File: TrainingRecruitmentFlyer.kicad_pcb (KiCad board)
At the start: 2 copper layers, 59.7 x 95.5 mm, 188 parts, among them SW1 3P1T_Fused, U1 VNH5019A-E, U10 LS_4, U2 VNH5019A-E, U3 3.3V_OKI, U4 LS_1, U5 LS_2, U6 TM4C129E_Launchpad_X9, U7 Picoblade-3, U8 Picoblade-3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

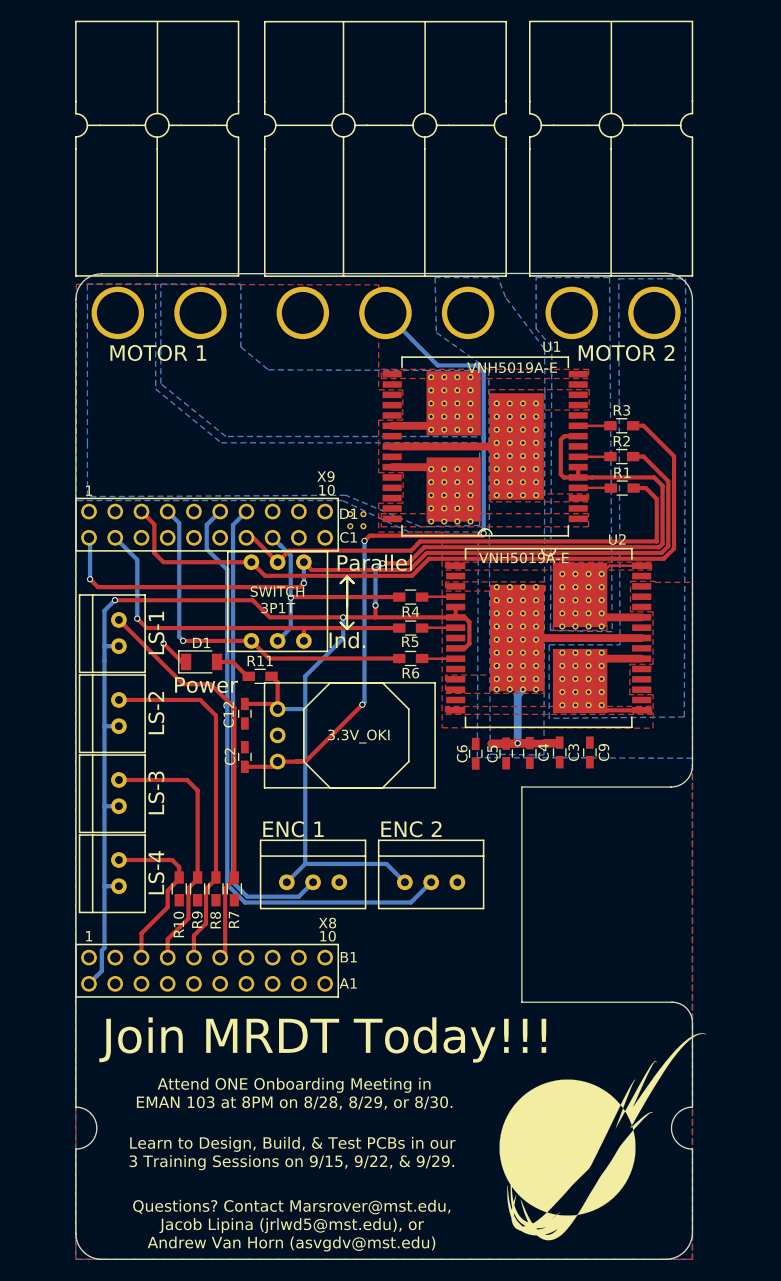
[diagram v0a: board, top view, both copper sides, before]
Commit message: Updated silkscreen, renamed files
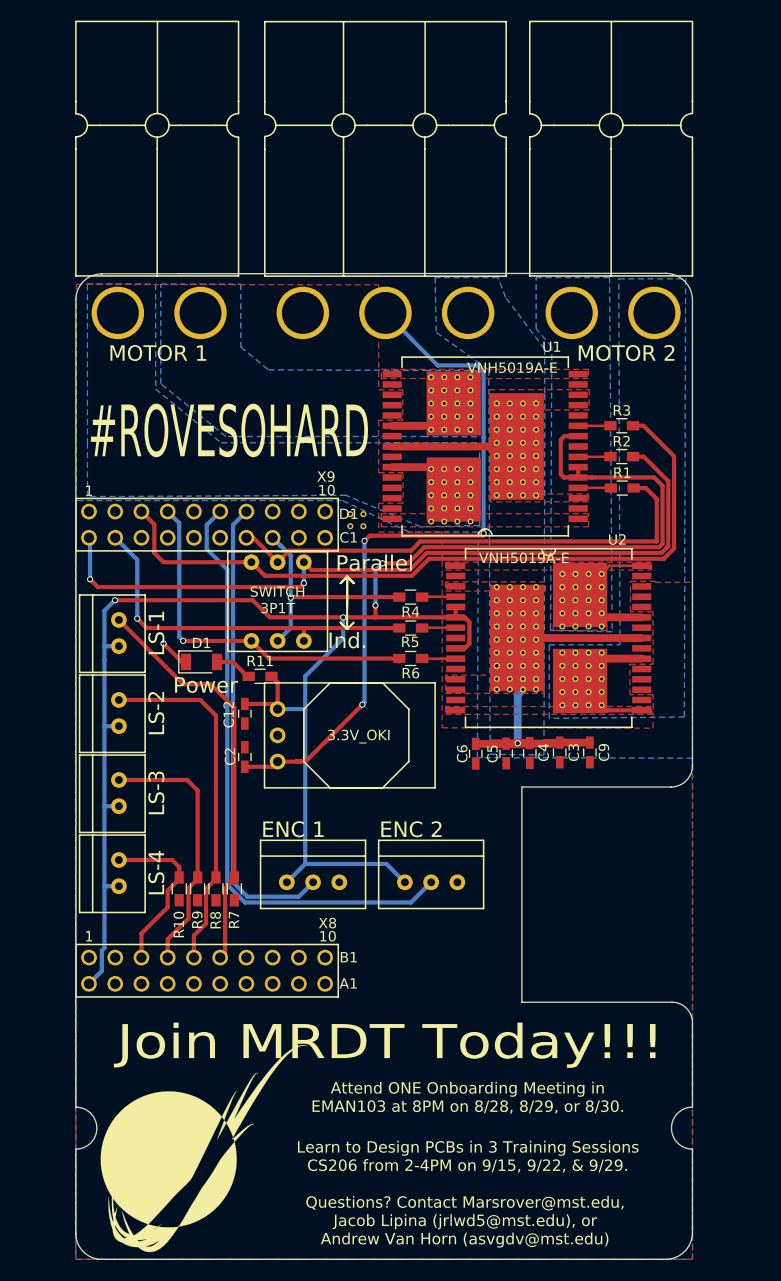
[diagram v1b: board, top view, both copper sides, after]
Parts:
- moved G*** 38.6 mm to (130.4, 223.3)
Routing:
- net +12V: track 41.0 -> 45.4 mm
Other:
- board text added: "#ROVESOHARD"
- board text added: "Attend ONE Onboarding Meeting in EMAN103 at 8PM on 8/28, 8/29, or 8/30."
- board text added: "Learn to Design PCBs in 3 Training Sessions CS206 from 2-4PM on 9/15, 9/22, & 9/29."
- board text added: "MARS ROVER DESIGN TEAM"
- board text added: "Today. Tomorrow. Forever."
- board text removed: "Attend ONE Onboarding Meeting in EMAN 103 at 8PM on 8/28, 8/29, or 8/30."
- board text removed: "Learn to Design, Build, & Test PCBs in our 3 Training Sessions on 9/15, 9/22, & 9/29."
- board text removed: "MARS ROVER DESIGN TEAM Today. Tomorrow. Forever"
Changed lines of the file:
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@@
 (kicad_pcb (version 4) (host pcbnew 4.0.7)
   (general
-    (links 0)
+    (links 259)
     (no_connects 2)
-    (area 117.958399 138.481599 177.748401 234.034801)
+    (area 116.32154 81.433999 192.4064 235.47846)
     (thickness 1.6)
-    (drawings 61)
-    (tracks 261)
+    (drawings 63)
+    (tracks 264)
     (zones 0)
     (modules 188)
@@
   )
   (setup
-    (last_trace_width 0.25)
+    (last_trace_width 0.762)
     (user_trace_width 0.254)
     (user_trace_width 0.4064)
@@
   )
   (module MRDT_Silkscreens:MRDT_Logo_20mm (layer F.Cu)
-    (at 169.037 222.123)
+    (at 130.429 223.266)
     (tags "Logo, MRDT")
     (fp_text reference G*** (at -3.6068 11.8364) (layer Dwgs.User) hide
@@
       (xy 9.693896 -10.010636)) (layer F.SilkS) (width 0.01))
   )
-  (gr_text "Questions? Contact Marsrover@mst.edu,\nJacob Lipina (jrlwd5@mst.edu), or\nAndrew Van Horn (asvgdv@mst.edu)" (at 138.938 230.632) (layer F.SilkS)
+  (gr_text "Today. Tomorrow. Forever." (at 147.955 157.226) (layer B.SilkS)
+    (effects (font (size 3 2.9) (thickness 0.3)) (justify mirror))
+  )
+  (gr_text "#ROVESOHARD" (at 132.842 153.924) (layer F.SilkS)
+    (effects (font (size 5 2.5) (thickness 0.3)))
+  )
+  (gr_text "Questions? Contact Marsrover@mst.edu,\nJacob Lipina (jrlwd5@mst.edu), or\nAndrew Van Horn (asvgdv@mst.edu)" (at 155.702 230.251) (layer F.SilkS)
     (effects (font (size 1.1 1.1) (thickness 0.275)))
   )
-  (gr_text "Learn to Design, Build, & Test PCBs in our\n3 Training Sessions on 9/15, 9/22, & 9/29." (at 138.938 223.647) (layer F.SilkS)
+  (gr_text "Learn to Design PCBs in 3 Training Sessions\nCS206 from 2-4PM on 9/15, 9/22, & 9/29." (at 155.956 224.028) (layer F.SilkS)
     (effects (font (size 1.1 1.1) (thickness 0.275)))
   )
-  (gr_text "Attend ONE Onboarding Meeting in\nEMAN 103 at 8PM on 8/28, 8/29, or 8/30." (at 139.192 217.932) (layer F.SilkS)
+  (gr_text "Attend ONE Onboarding Meeting in\nEMAN103 at 8PM on 8/28, 8/29, or 8/30." (at 155.956 218.313) (layer F.SilkS)
     (effects (font (size 1.1 1.1) (thickness 0.25)))
   )
-  (gr_text "Join MRDT Today!!!" (at 142.367 212.471) (layer F.SilkS)
-    (effects (font (size 3.3 3.3) (thickness 0.3)))
+  (gr_text "Join MRDT Today!!!" (at 148.463 212.979) (layer F.SilkS)
+    (effects (font (size 3.3 4) (thickness 0.3)))
   )
-  (gr_text "MARS ROVER DESIGN TEAM\nToday. Tomorrow. Forever" (at 147.574 153.924) (layer B.SilkS)
-    (effects (font (size 2.9 2.9) (thickness 0.3)) (justify mirror))
+  (gr_text "MARS ROVER DESIGN TEAM" (at 147.828 151.765) (layer B.SilkS)
+    (effects (font (size 5 2.9) (thickness 0.3)) (justify mirror))
   )
   (gr_text ACT (at 156.083 146.304) (layer B.SilkS)
@@
   (segment (start 155.65501 171.837599) (end 154.7749 171.837599) (width 0.4064) (layer F.Cu) (net 2))
   (segment (start 154.7749 170.837601) (end 154.7749 171.837599) (width 0.4064) (layer F.Cu) (net 2))
+  (segment (start 164.846 183.962) (end 167.767 183.962) (width 0.762) (layer F.Cu) (net 3))
+  (segment (start 158.242 184.0636) (end 158.2166 184.089) (width 0.762) (layer F.Cu) (net 3))
+  (segment (start 158.2166 184.089) (end 156.718 184.089) (width 0.762) (layer F.Cu) (net 3))
   (segment (start 158.242 184.0636) (end 159.6644 184.0636) (width 0.762) (layer F.Cu) (net 3))
   (segment (start 159.6644 184.0636) (end 160.7414 184.0636) (width 0.762) (layer F.Cu) (net 3))

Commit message: Changed text to pass ACT
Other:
- board text added: "Learn to Design PCBs in THREE Sessions CS206 from 2-4PM on 9/15, 9/22, & 9/29."
- board text removed: "Learn to Design PCBs in 3 Training Sessions CS206 from 2-4PM on 9/15, 9/22, & 9/29."
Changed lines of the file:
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@@
   (general
     (links 259)
-    (no_connects 2)
-    (area 116.32154 81.433999 192.4064 235.47846)
+    (no_connects 0)
+    (area 116.32154 81.433999 192.4064 236.62146)
     (thickness 1.6)
     (drawings 63)
@@
   )
   (setup
-    (last_trace_width 0.762)
+    (last_trace_width 0.25)
     (user_trace_width 0.254)
     (user_trace_width 0.4064)
@@
     (effects (font (size 1.1 1.1) (thickness 0.275)))
   )
-  (gr_text "Learn to Design PCBs in 3 Training Sessions\nCS206 from 2-4PM on 9/15, 9/22, & 9/29." (at 155.956 224.028) (layer F.SilkS)
+  (gr_text "Learn to Design PCBs in THREE Sessions\nCS206 from 2-4PM on 9/15, 9/22, & 9/29." (at 155.956 224.028) (layer F.SilkS)
     (effects (font (size 1.1 1.1) (thickness 0.275)))
   )

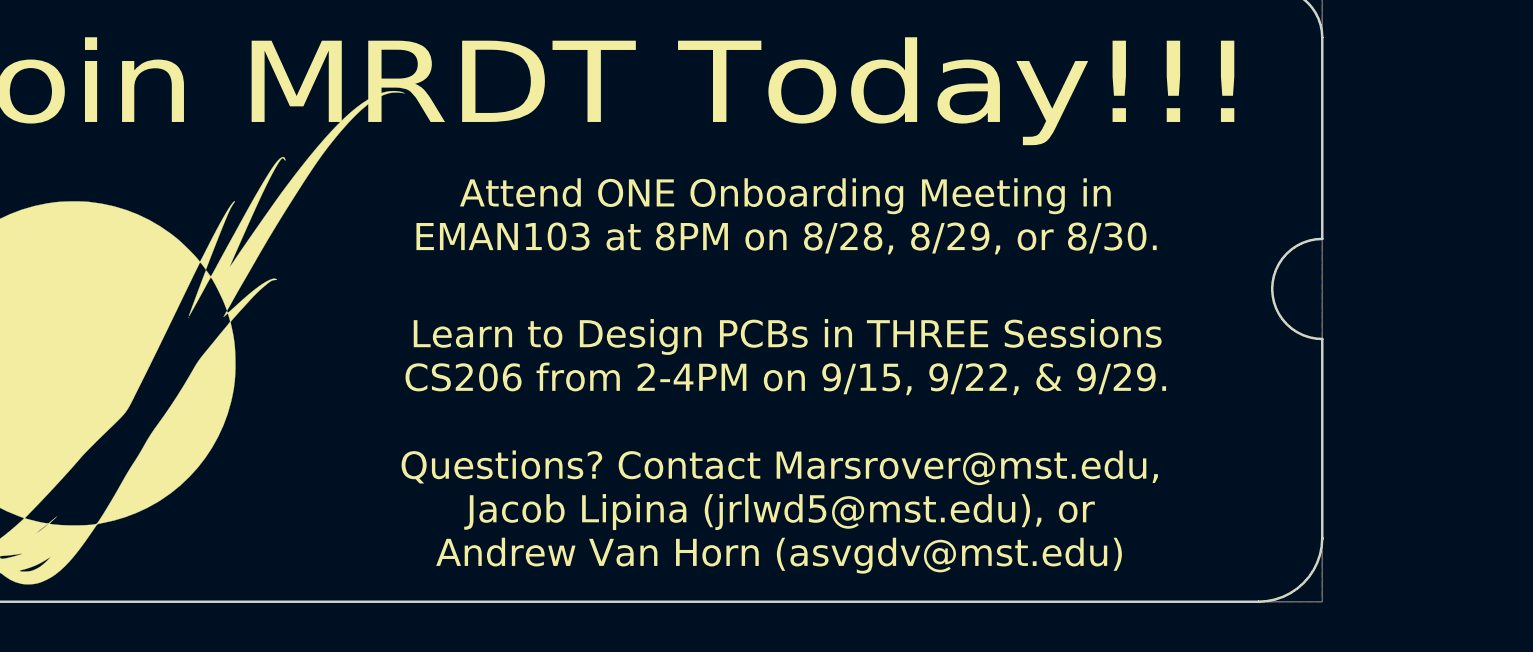
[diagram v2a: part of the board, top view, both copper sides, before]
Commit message: Modified silkscreen test and re-generated Gerbs
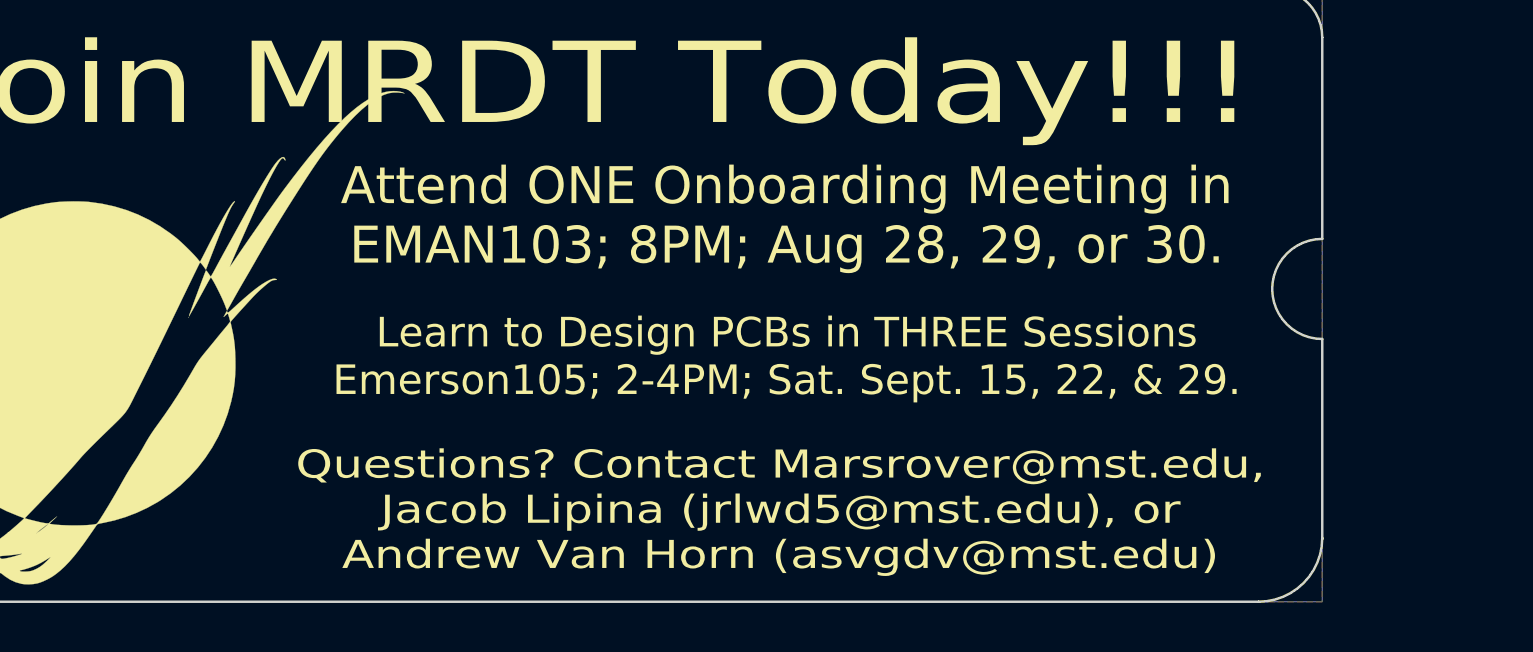
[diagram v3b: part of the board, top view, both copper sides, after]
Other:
- board text added: "Attend ONE Onboarding Meeting in EMAN103; 8PM; Aug 28, 29, or 30."
- board text added: "Learn to Design PCBs in THREE Sessions Emerson105; 2-4PM; Sat. Sept. 15, 22, & 29."
- board text removed: "Attend ONE Onboarding Meeting in EMAN103 at 8PM on 8/28, 8/29, or 8/30."
- board text removed: "Learn to Design PCBs in THREE Sessions CS206 from 2-4PM on 9/15, 9/22, & 9/29."
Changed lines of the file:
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@@
     (links 259)
     (no_connects 0)
-    (area 116.32154 81.433999 192.4064 236.62146)
+    (area 117.958399 138.481599 177.748401 234.034801)
     (thickness 1.6)
     (drawings 63)
@@
   )
   (gr_text "Questions? Contact Marsrover@mst.edu,\nJacob Lipina (jrlwd5@mst.edu), or\nAndrew Van Horn (asvgdv@mst.edu)" (at 155.702 230.251) (layer F.SilkS)
-    (effects (font (size 1.1 1.1) (thickness 0.275)))
+    (effects (font (size 1.14 1.4) (thickness 0.275)))
   )
-  (gr_text "Learn to Design PCBs in THREE Sessions\nCS206 from 2-4PM on 9/15, 9/22, & 9/29." (at 155.956 224.028) (layer F.SilkS)
-    (effects (font (size 1.1 1.1) (thickness 0.275)))
+  (gr_text "Learn to Design PCBs in THREE Sessions\nEmerson105; 2-4PM; Sat. Sept. 15, 22, & 29." (at 155.956 224.028) (layer F.SilkS)
+    (effects (font (size 1.2 1.2) (thickness 0.275)))
   )
-  (gr_text "Attend ONE Onboarding Meeting in\nEMAN103 at 8PM on 8/28, 8/29, or 8/30." (at 155.956 218.313) (layer F.SilkS)
-    (effects (font (size 1.1 1.1) (thickness 0.25)))
+  (gr_text "Attend ONE Onboarding Meeting in\nEMAN103; 8PM; Aug 28, 29, or 30." (at 155.956 218.313) (layer F.SilkS)
+    (effects (font (size 1.5 1.5) (thickness 0.25)))
   )
   (gr_text "Join MRDT Today!!!" (at 148.463 212.979) (layer F.SilkS)
